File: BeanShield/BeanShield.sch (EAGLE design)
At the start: 8 parts, among them IC1 78L24Z

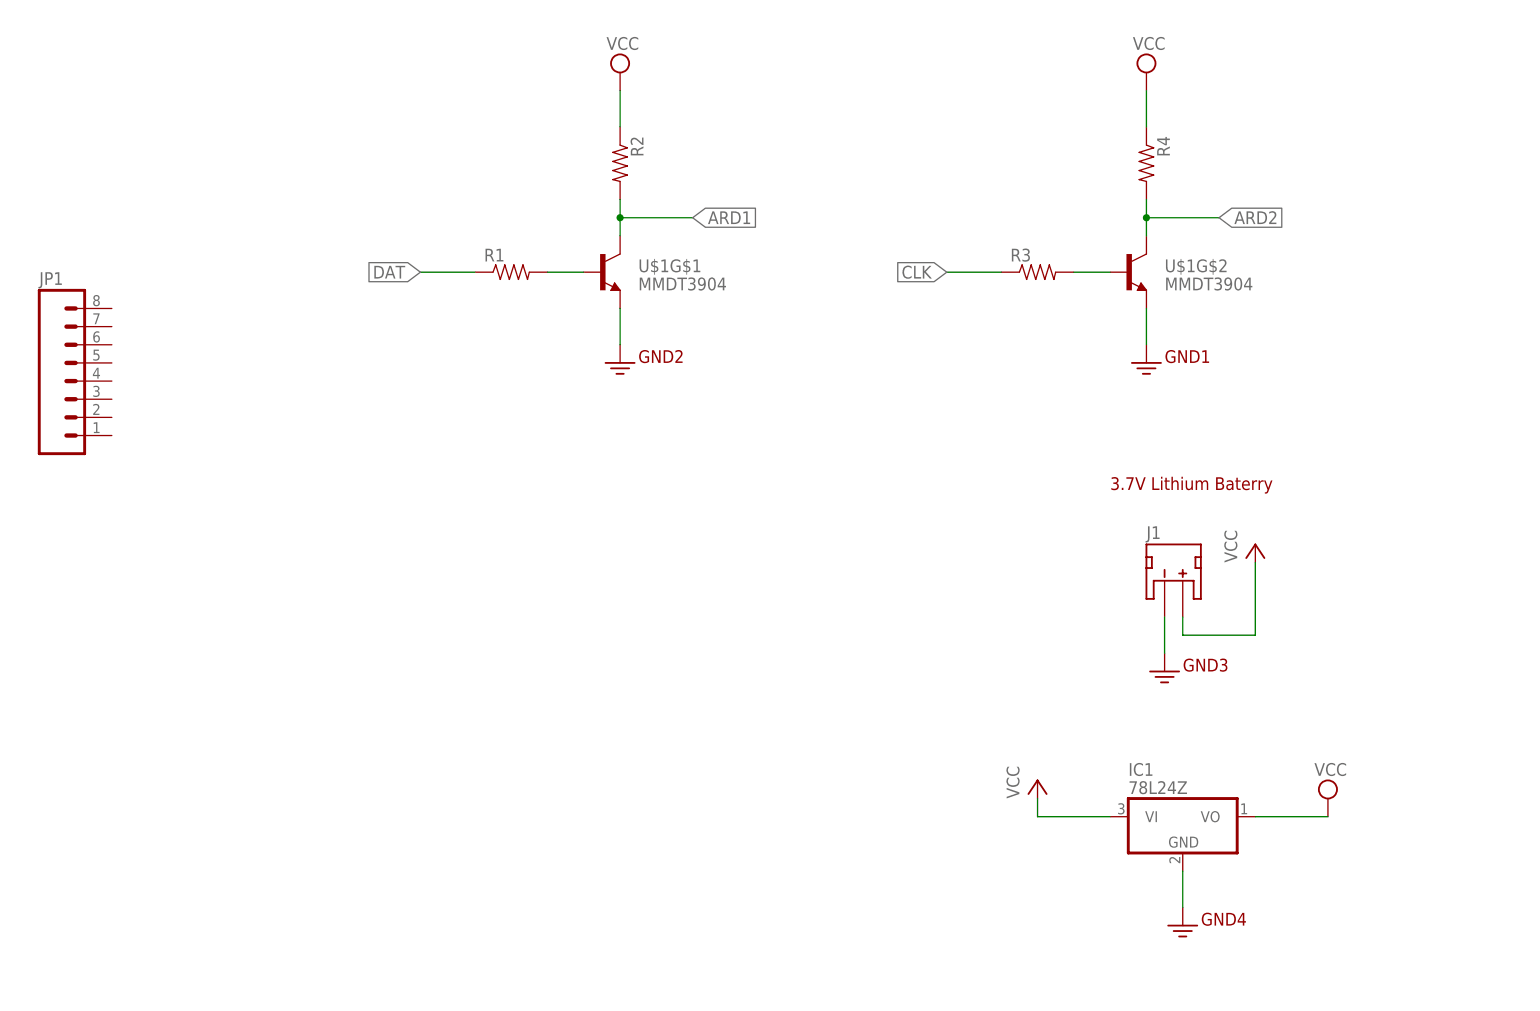
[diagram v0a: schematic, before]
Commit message: added logotype to frame
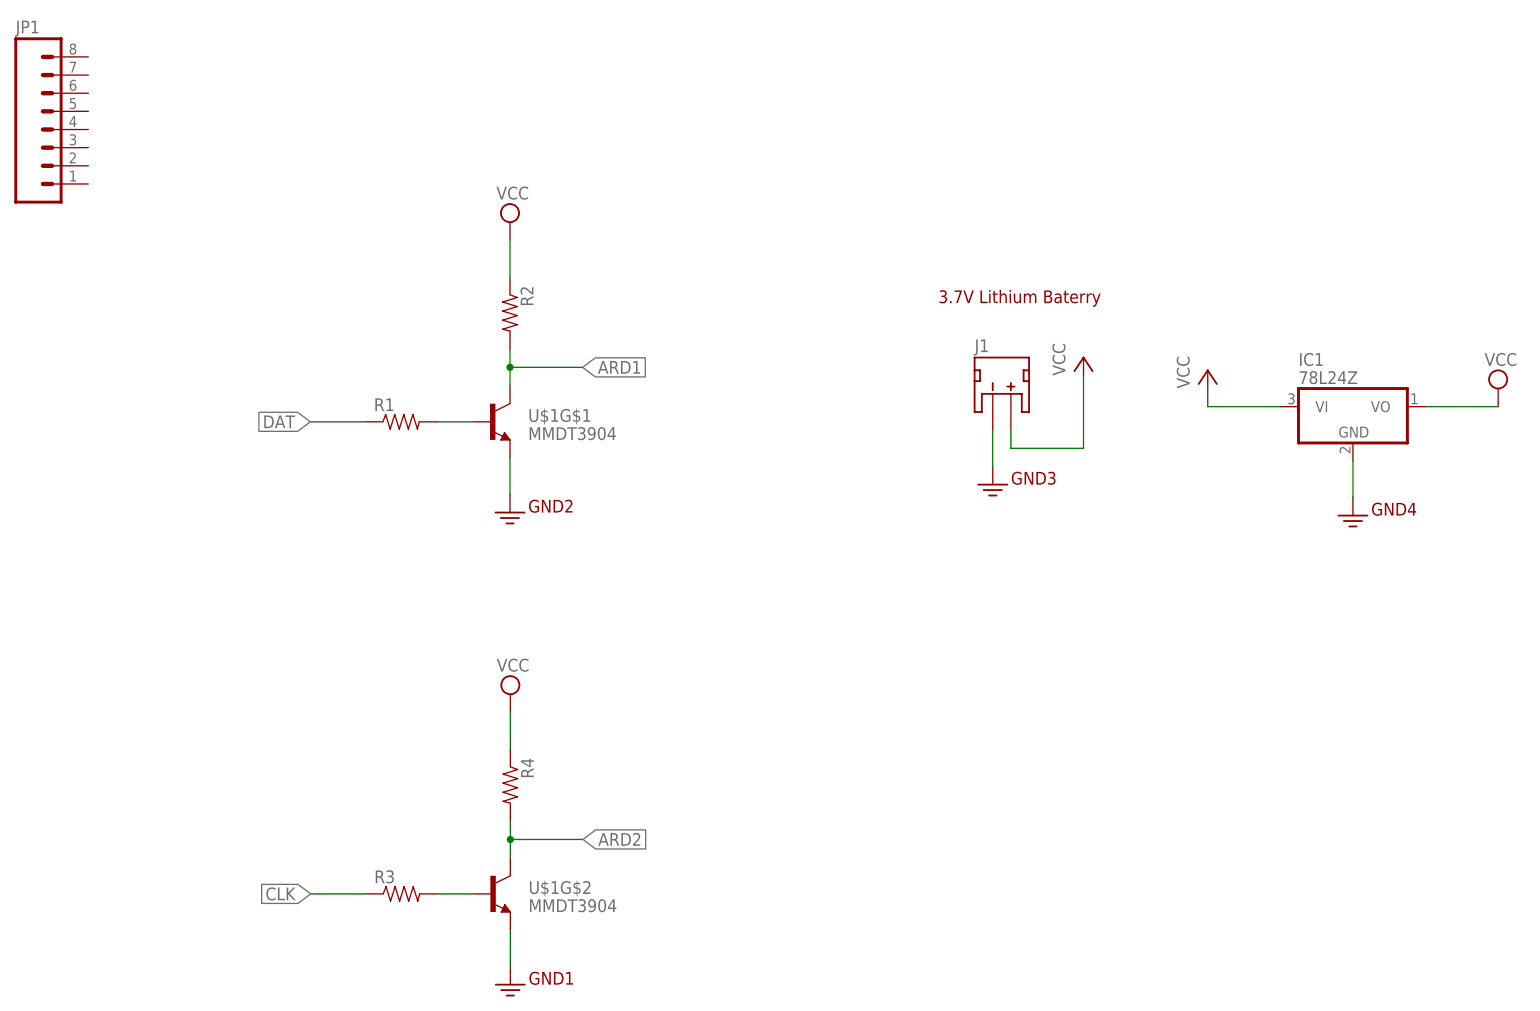
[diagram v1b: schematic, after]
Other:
- note added: "/Users/oaf7862/Documents/eagle_fetlab.bmp"
- moved on the sheet: IC1, J1, JP1, R1, R2, R3, R4, U$1G$1, U$1G$2
